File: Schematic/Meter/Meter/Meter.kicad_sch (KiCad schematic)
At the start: 7 parts

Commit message: update
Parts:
- added BT?: Battery, symbol Device:Battery
- added J?: SD Card Module, symbol Connector:Conn_01x06_Male
- added L? (x3): Solenoid, symbol pspice:INDUCTOR
- added Q? (x3): IRLZ44N, Package_TO_SOT_THT:TO-220-3_Vertical, symbol Transistor_FET:IRLZ44N
- added U?: L7805, symbol Regulator_Linear:L7805
- added U?: NRF24L01_Breakout, RF_Module:nRF24L01_Breakout, symbol RF:NRF24L01_Breakout
- added U?: LM2596, symbol Regulator_Linear:LM1117-3.3
- J? (x3): value Conn_01x03_Male -> Flow Sensor
- J?: value Conn_01x04_Male -> I2C LCD
- J?: value Conn_01x08_Male -> Keypad

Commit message: update
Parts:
- removed J? (x2): Flow Sensor, symbol Connector:Conn_01x03_Male
- removed L? (x2): Solenoid, symbol pspice:INDUCTOR
- removed Q? (x2): IRLZ44N, Package_TO_SOT_THT:TO-220-3_Vertical, symbol Transistor_FET:IRLZ44N
- removed U?: L7805, symbol Regulator_Linear:L7805
- added D?: DIODE, symbol pspice:DIODE
- added J? (x2): Flow Sensor, symbol Connector:Conn_01x03_Male
- added R? (x2): R, symbol Device:R
- added U?: LM2596, symbol Regulator_Linear:LM1117-3.3
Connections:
- net 5V: now reaches J?.1 (Pin_1)
- net 5V: now also A?.27 (+5V), J?.1 (Pin_1), J?.1 (Pin_1), J?.1 (Pin_1), U?.2 (VO)
- net SDA: now reaches J?.2 (Pin_2)
- net SDA: now also U?.33 (IO21)
- net SCL: now reaches J?.3 (Pin_3)
- net SCL: now also U?.36 (IO22)
- net GND: now reaches J?.4 (Pin_4)
- net GND: now also A?.29 (GND), A?.4 (GND), BT?.2 (-), J?.3 (Pin_3), J?.6 (Pin_6), U?.1 (GND), U?.1 (GND), U?.1 (GND), U?.15 (GND), U?.38 (GND), U?.39 (GND), J?.3 (Pin_3), J?.3 (Pin_3), U?.1 (GND)
- net 3.3V: now reaches J?.1 (Pin_1)
- net 3.3V: now also U?.2 (VCC), U?.2 (VO)
- net D13: now reaches J?.2 (Pin_2)
- net D13: now also A?.16 (D13)
- net D12: now reaches J?.3 (Pin_3)
- net D12: now also A?.15 (D12)
- net D11: now reaches J?.4 (Pin_4)
- net D11: now also A?.14 (D11)
- net D10: now reaches J?.5 (Pin_5)
- net D10: now also A?.13 (D10)
- net RX2: now reaches A?.10 (D7)
- net RX2: now also U?.27 (IO16)
- net A2: now reaches A?.21 (A2)
- net A3: now reaches A?.22 (A3)
- net A4: now reaches A?.23 (A4)
- net D3: now reaches A?.6 (D3)
- net D3: now also J?.2 (Pin_2)
- net D4: now reaches A?.7 (D4)
- net D4: now also J?.2 (Pin_2)
- net D5: now reaches A?.8 (D5)
- net D5: now also J?.2 (Pin_2)
- net TX2: now reaches A?.9 (D6)
- net TX2: now also U?.28 (IO17)
- net IO4: now reaches J?.1 (Pin_1)
- net IO4: now also U?.26 (IO4)
- net IO13: now reaches J?.2 (Pin_2)
- net IO13: now also U?.16 (IO13)
- net IO14: now reaches J?.3 (Pin_3)
- net IO14: now also U?.13 (IO14)
- net IO25: now reaches J?.4 (Pin_4)
- net IO25: now also U?.10 (IO25)
- net IO26: now reaches J?.5 (Pin_5)
- net IO26: now also U?.11 (IO26)
- net IO27: now reaches J?.6 (Pin_6)
- net IO32: now reaches J?.7 (Pin_7)
- net IO32: now also U?.8 (IO32)
- net IO33: now reaches J?.8 (Pin_8)
- net IO33: now also U?.9 (IO33)
- net IO15: now reaches U?.3 (CE)
- net IO15: now also U?.23 (IO15)
- net IO5: now reaches U?.4 (~{CSN})
- net IO5: now also U?.29 (IO5)
- net IO18: now reaches U?.5 (SCK)
- net IO18: now also U?.30 (IO18)
- net IO23: now reaches U?.6 (MOSI)
- net IO23: now also U?.37 (IO23)
- net IO19: now reaches U?.7 (MISO)
- net IO19: now also U?.31 (IO19)
- net at U?.3 (VI): now also BT?.1 (+), U?.3 (VI)
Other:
- moved on the sheet: A?, BT?, J?, L?, Q?, U?

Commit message: update
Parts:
- added R3: 1k, symbol Device:R
- added R4: 2k, symbol Device:R
- gave numbers to parts that had none: 17
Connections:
- net GND: now also R4.2
- net RX2: now also R3.2, R4.1; no longer A1.10 (D7)
- new net: A1.10 (D7), R3.1
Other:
- note added: "SS_RX"
- note added: "SS_TX"

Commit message: update
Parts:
- added C1: 470uF, symbol Device:C_Polarized_Small
- added C2: 100uF, symbol Device:C_Polarized_Small
- added D2, D3: (no value), symbol pspice:DIODE
- added L2, L3: Solenoid, symbol pspice:INDUCTOR
- added Q2, Q3: IRLZ44N, Package_TO_SOT_THT:TO-220-3_Vertical, symbol Transistor_FET:IRLZ44N
- added R5, R6: 10k, symbol Device:R
- added R7, R8: 220R, symbol Device:R
- added U5: L7809, symbol Regulator_Linear:LM1117-3.3
- added U6: L7805, symbol Regulator_Linear:LM1117-3.3
- BT1: value Battery -> 16.8V
- D1: value DIODE -> (none)
- R1: value R -> 10k
- R2: value R -> 220R
- U1: value NRF24L01_Breakout -> NRF24L01
- renumbered J3 to J1, J1 to J3, J5 to J4, J6 to J5, J4 to J6
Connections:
- net 3.3V: now also U3.2 (VO), U4.2 (VDD); no longer U2.2 (VO)
- net 5V: now also U6.2 (VO); no longer U3.2 (VO)
- net A2: now also R1.1, R2.1
- net A3: now also R6.1, R8.1
- net A4: now also R5.1, R7.1
- net GND: now also Q1.3 (S), R1.2, C1.2, C2.2, Q2.3 (S), Q3.3 (S), R5.2, R6.2, U5.1 (GND), U6.1 (GND)
- net at D1.1 (K): now also L1.2, Q1.2 (D)
- net 12V: now reaches D1.2 (A)
- net 12V: now also L1.1, U2.2 (VO), C1.1, D2.2 (A), D3.2 (A), L2.1, L3.1, U5.3 (VI)
- net at R2.2: now also Q1.1 (G)
- new net: D2.1 (K), L2.2, Q2.2 (D)
- new net: Q3.1 (G), R8.2
- new net: D3.1 (K), L3.2, Q3.2 (D)
- new net: Q2.1 (G), R7.2
- new net 9V: C2.1, U5.2 (VO), U6.3 (VI)
- no-connect marks 0 -> 33
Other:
- note added: "SMART WATER METER"
- moved on the sheet: A1, BT1, D1, J1, J2, J3, J4, J5, J6, L1, Q1, R1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

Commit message: added schematic for smart meter
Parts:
- renumbered D3 to D2, D2 to D3, L3 to L2, L2 to L3, Q3 to Q2, Q2 to Q3
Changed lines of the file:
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@@
   (symbol (lib_id "pspice:DIODE") (at 53.848 142.367 90) (unit 1)
     (in_bom yes) (on_board yes)
-    (property "Reference" "D2" (id 0) (at 57.023 141.4585 90)
+    (property "Reference" "D3" (id 0) (at 57.023 141.4585 90)
       (effects (font (size 1.27 1.27)) (justify right))
     )
@@
   (symbol (lib_id "Transistor_FET:IRLZ44N") (at 57.912 111.76 0) (unit 1)
     (in_bom yes) (on_board yes) (fields_autoplaced)
-    (property "Reference" "Q3" (id 0) (at 63.119 110.8515 0)
+    (property "Reference" "Q2" (id 0) (at 63.119 110.8515 0)
       (effects (font (size 1.27 1.27)) (justify left))
     )
@@
   (symbol (lib_id "pspice:INDUCTOR") (at 60.452 97.917 270) (unit 1)
     (in_bom yes) (on_board yes) (fields_autoplaced)
-    (property "Reference" "L3" (id 0) (at 62.357 97.0085 90)
+    (property "Reference" "L2" (id 0) (at 62.357 97.0085 90)
       (effects (font (size 1.27 1.27)) (justify left))
     )
@@
   (symbol (lib_id "pspice:DIODE") (at 53.975 99.314 90) (unit 1)
     (in_bom yes) (on_board yes)
-    (property "Reference" "D3" (id 0) (at 57.15 98.4055 90)
+    (property "Reference" "D2" (id 0) (at 57.15 98.4055 90)
       (effects (font (size 1.27 1.27)) (justify right))
     )
@@
   (symbol (lib_id "pspice:INDUCTOR") (at 60.325 140.97 270) (unit 1)
     (in_bom yes) (on_board yes) (fields_autoplaced)
-    (property "Reference" "L2" (id 0) (at 62.23 140.0615 90)
+    (property "Reference" "L3" (id 0) (at 62.23 140.0615 90)
       (effects (font (size 1.27 1.27)) (justify left))
     )
@@
   (symbol (lib_id "Transistor_FET:IRLZ44N") (at 57.785 154.813 0) (unit 1)
     (in_bom yes) (on_board yes) (fields_autoplaced)
-    (property "Reference" "Q2" (id 0) (at 62.992 153.9045 0)
+    (property "Reference" "Q3" (id 0) (at 62.992 153.9045 0)
       (effects (font (size 1.27 1.27)) (justify left))
     )
@@
       (reference "D1") (unit 1) (value " ") (footprint "")
     )
+    (path "/9032d26a-aef4-49b7-beb7-322cf95ed8fd"
+      (reference "D2") (unit 1) (value " ") (footprint "")
+    )
     (path "/50486944-6c76-467e-8ea6-3e60b0873eb0"
-      (reference "D2") (unit 1) (value " ") (footprint "")
-    )
-    (path "/9032d26a-aef4-49b7-beb7-322cf95ed8fd"
       (reference "D3") (unit 1) (value " ") (footprint "")
     )
@@
       (reference "L1") (unit 1) (value "Solenoid") (footprint "")
     )
+    (path "/8c6d6042-b985-410c-a32a-44bd3d2d480e"
+      (reference "L2") (unit 1) (value "Solenoid") (footprint "")
+    )
     (path "/cd36f50f-9421-4500-850b-f8ea7b7935a1"
-      (reference "L2") (unit 1) (value "Solenoid") (footprint "")
-    )
-    (path "/8c6d6042-b985-410c-a32a-44bd3d2d480e"
       (reference "L3") (unit 1) (value "Solenoid") (footprint "")
     )
@@
       (reference "Q1") (unit 1) (value "IRLZ44N") (footprint "Package_TO_SOT_THT:TO-220-3_Vertical")
     )
+    (path "/51870781-7260-49e7-a4dc-72a5ab15ecbc"
+      (reference "Q2") (unit 1) (value "IRLZ44N") (footprint "Package_TO_SOT_THT:TO-220-3_Vertical")
+    )
     (path "/e23dc053-8a72-4ba5-b335-8d2c550fc130"
-      (reference "Q2") (unit 1) (value "IRLZ44N") (footprint "Package_TO_SOT_THT:TO-220-3_Vertical")
-    )
-    (path "/51870781-7260-49e7-a4dc-72a5ab15ecbc"
       (reference "Q3") (unit 1) (value "IRLZ44N") (footprint "Package_TO_SOT_THT:TO-220-3_Vertical")
     )

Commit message: update
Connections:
- net 3.3V: no longer J6.1 (Pin_1)
- net 5V: now also J6.1 (Pin_1)
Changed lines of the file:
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@@
     (effects (font (size 1.27 1.27)) (justify left bottom))
   )
-  (label "3.3V" (at 212.598 128.27 0)
+  (label "5V" (at 212.598 128.27 0)
     (effects (font (size 1.27 1.27)) (justify left bottom))
   )

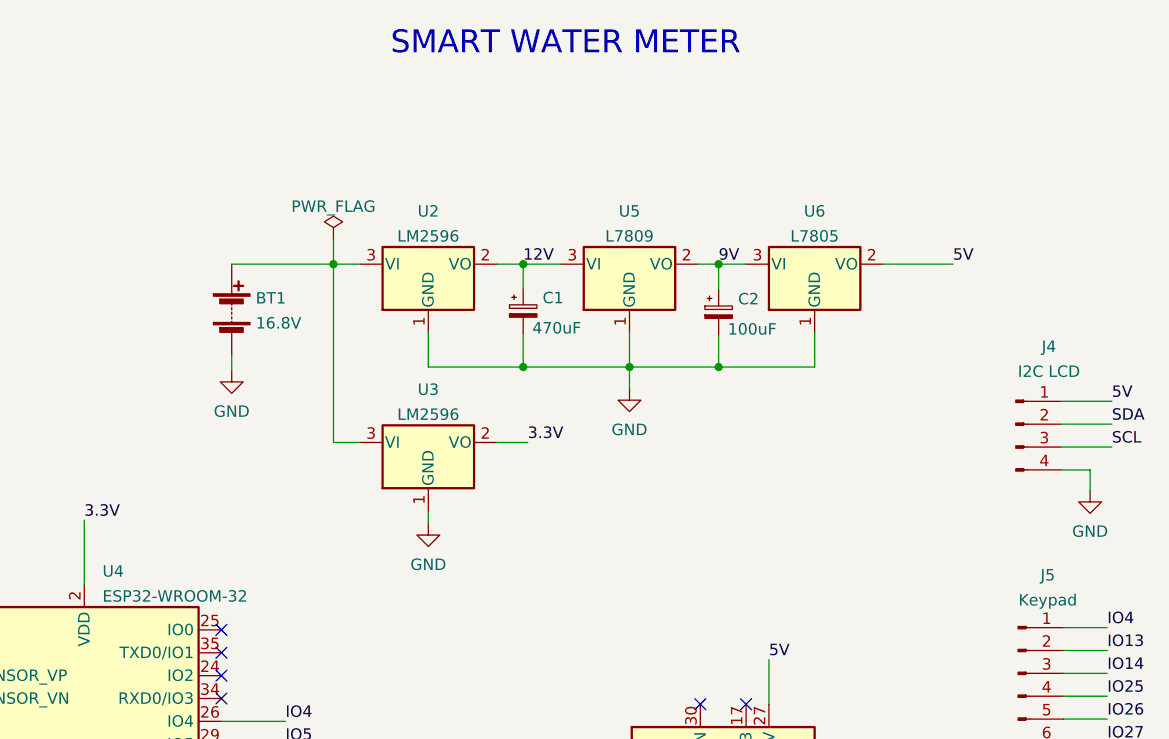
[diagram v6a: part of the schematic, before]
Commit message: schematic update
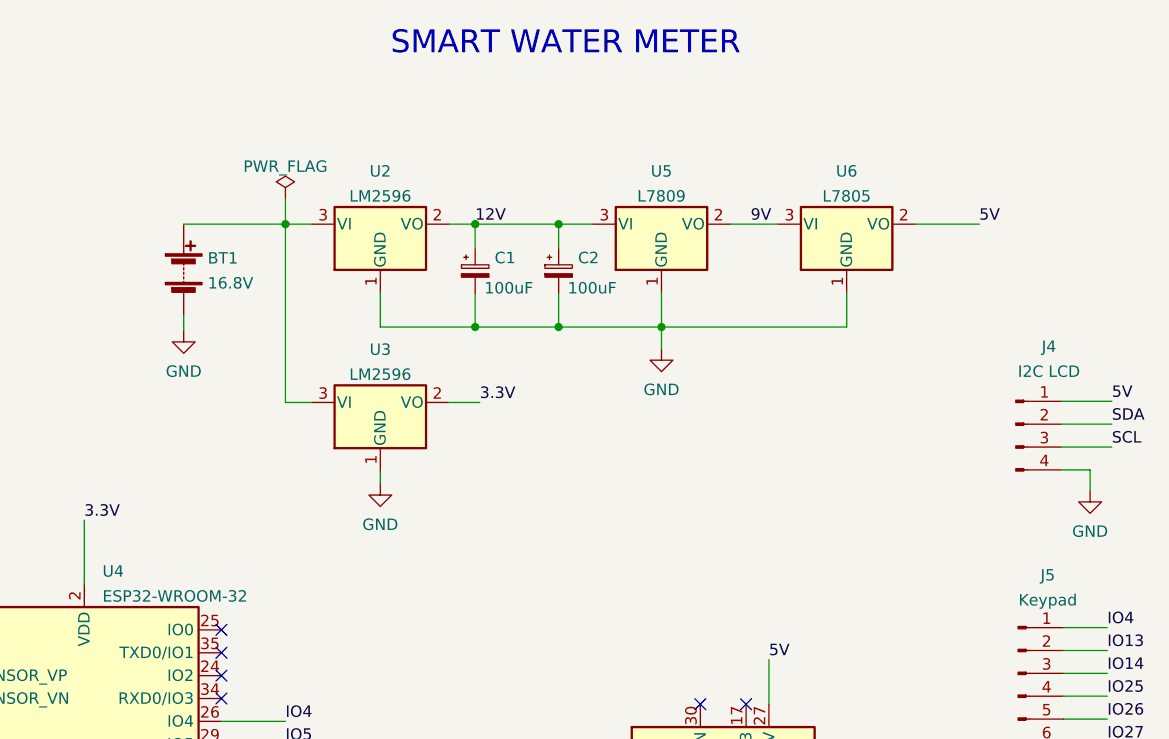
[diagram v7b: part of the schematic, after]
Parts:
- C1: value 470uF -> 100uF
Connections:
- net 12V: now also C2.1
- net 9V: no longer C2.1
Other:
- moved on the sheet: BT1, C1, U2, U3, U5, U6
